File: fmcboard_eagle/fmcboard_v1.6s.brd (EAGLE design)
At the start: 147 x 74 mm, 300 parts, among them IC1 OPA699ID, IC10 LM358, IC11 7805DT, IC12 SN74AUC2G66DCTR, IC13 SN74AUC2G66DCTR, IC14 SN74AUC2G66DCTR, IC15 SN74AUC2G66DCTR, IC16 DAC7578SPWR, IC17 SN74AUC2G66DCTR, IC18 SN74AUC2G66DCTR, IC19 SN74AUC2G66DCTR, IC2 DAC7578SPWR, IC20 SN74AUC2G66DCTR, IC21 74AUP2GU04GW, IC22 74AUP2GU04GW, IC23 74AUP2GU04GW, IC24 74AUP2GU04GW, IC25 MC7905ACD2TR4G, IC26 AMS1117-1.8, IC27 LM358, IC28 SN74AUC2G66DCTR, IC29 LM337KVURG3, IC3 LTC6229IMS8E#TRPBF, IC30 SN74AUC2G66DCTR, IC31 SN74AUC2G66DCTR, IC32 SN74AUC2G66DCTR, IC33 LTC6229IMS8E#TRPBF, IC34 74AUP2GU04GW, IC35 74AUP2GU04GW, IC36 TPS5430DDAR, IC37 TPS5430DDAR, IC4 OPA695IDR, IC5 LTC6229IMS8E#TRPBF, IC6 OPA695IDR, IC7 OPA699ID, IC8 LM358, IC9 LM358, J1 8pin, J12 4p-2.54, J13 4p-2.54, J2 ASP-134604-01, J3 2p-2.54, J4 4p-2.54, J5 4p-2.54, J8 4p-2.54, J9 2p-2.54

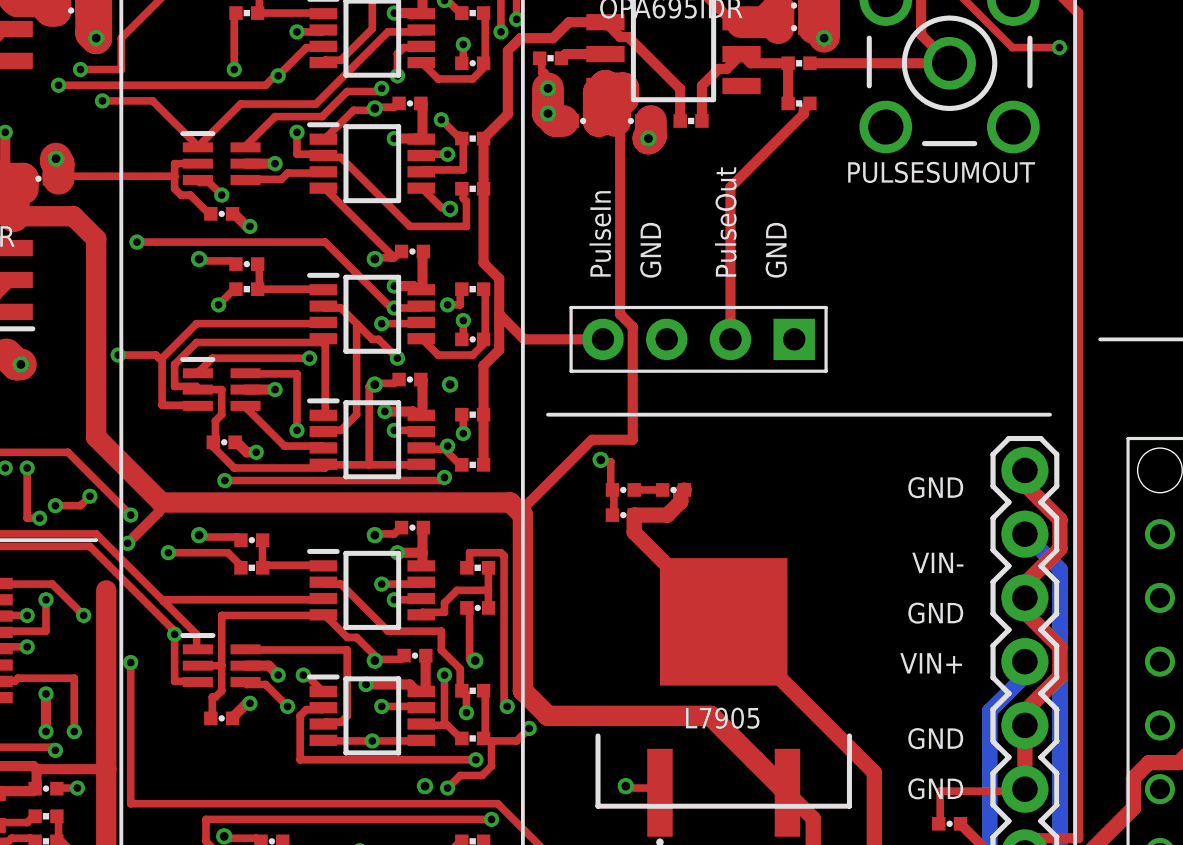
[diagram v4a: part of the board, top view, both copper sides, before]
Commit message: remove pulsein hole
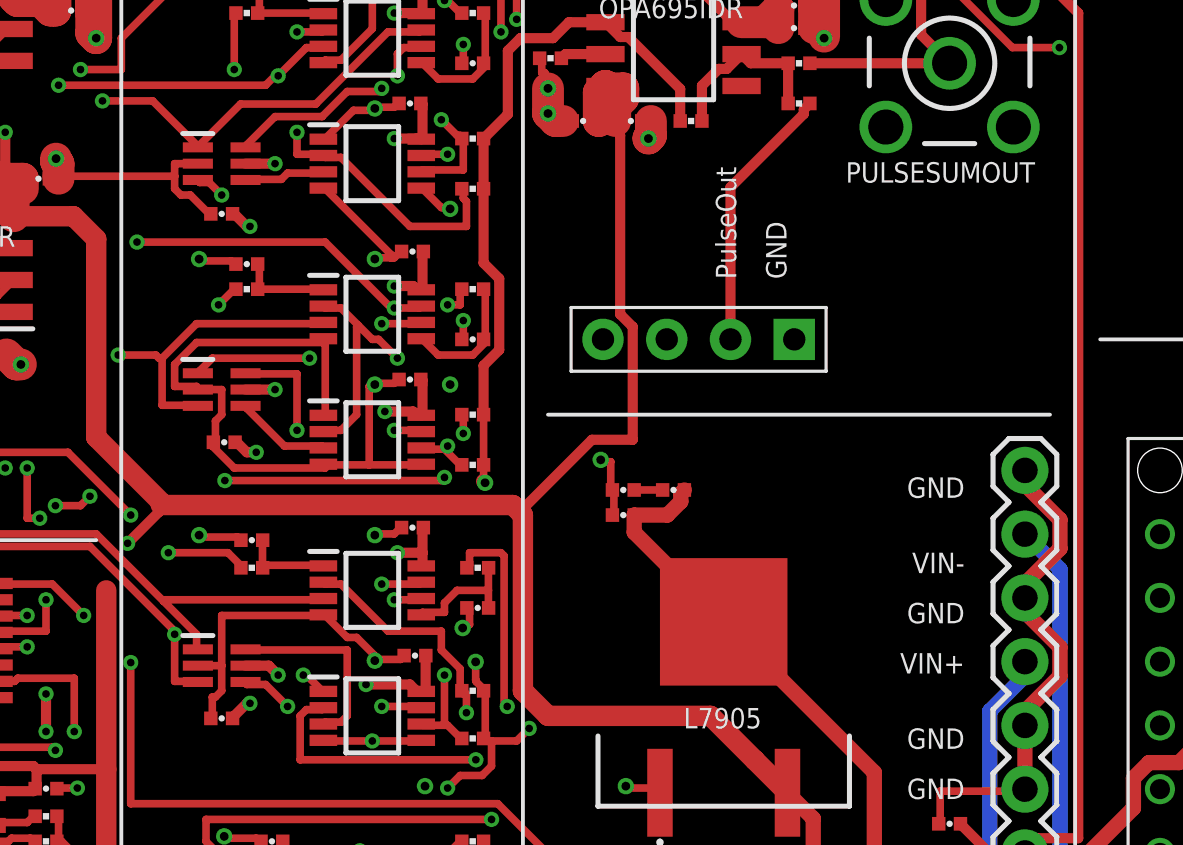
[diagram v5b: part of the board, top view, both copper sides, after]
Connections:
- net GND: no longer J13.3
- net PULSESUMIN: no longer J13.4
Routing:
- net PULSESUMIN: track 111.4 -> 108.3 mm, vias 6 -> 8
- net GND: track 529.4 -> 527.5 mm
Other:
- board text removed: "PulseIn"
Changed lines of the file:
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@@
 <text x="22.4" y="63.1" size="0.8128" layer="21" rot="R180">12V</text>
 <text x="100.6" y="35.5" size="0.8128" layer="21" rot="R180">GND</text>
-<text x="88.5" y="55.4" size="0.8128" layer="21" rot="R90">GND</text>
 <text x="100.6" y="47.5" size="0.8128" layer="21" rot="R180">GND</text>
 <text x="7" y="1" size="1.27" layer="21" rot="R90">C10GX FMC breakout, v1.652s
@@
 <text x="100.6" y="32.5" size="0.8128" layer="21" rot="R180">+VS 5</text>
 <text x="100.6" y="30.5" size="0.8128" layer="21" rot="R180">AR 5V</text>
-<text x="86.5" y="55.4" size="0.8128" layer="21" rot="R90">PulseIn</text>
 <text x="93.5" y="55.4" size="0.8128" layer="21" rot="R90">GND</text>
 <text x="91.5" y="55.4" size="0.8128" layer="21" rot="R90">PulseOut</text>
@@
 <contactref element="PULSESUMOUT" pad="5"/>
 <contactref element="PULSESUMOUT" pad="3"/>
-<contactref element="J1" pad="8"/>
 <contactref element="C6" pad="2"/>
 <contactref element="C15" pad="2"/>
@@
 <contactref element="C74" pad="2"/>
 <contactref element="J13" pad="1"/>
-<contactref element="J13" pad="3"/>
 <contactref element="J5" pad="4"/>
 <contactref element="R10" pad="1"/>
@@
 <wire x1="141.635" y1="41.365" x2="141" y2="42" width="0.6096" layer="1"/>
 <wire x1="104.397" y1="45.8186625" x2="104.397" y2="44.6613375" width="0.6096" layer="1"/>
-<wire x1="103" y1="47.78" x2="103" y2="47.2156625" width="0.6096" layer="1"/>
 <wire x1="103" y1="43.2643375" x2="103" y2="42.7" width="0.6096" layer="1"/>
 <wire x1="103" y1="47.2156625" x2="104.397" y2="45.8186625" width="0.6096" layer="1"/>
@@
 <via x="81.1" y="17.2" extent="1-16" drill="0.35"/>
 <via x="81.1" y="28.2" extent="1-16" drill="0.35"/>
-<via x="81.1" y="40.2" extent="1-16" drill="0.35"/>
+<via x="80.6" y="41.5" extent="1-16" drill="0.35"/>
 <via x="80.1" y="51.2" extent="1-16" drill="0.35"/>
 <via x="80.1" y="58.2" extent="1-16" drill="0.35"/>
@@
 <wire x1="78.125" y1="45.5" x2="78.16693125" y2="45.5" width="0.3048" layer="1"/>
 <wire x1="77.125" y1="45.25" x2="77.1" y2="45.2" width="0.3048" layer="1"/>
-<wire x1="80.875" y1="40.25" x2="80.875" y2="42.25" width="0.3048" layer="1"/>
-<wire x1="81" y1="40.25" x2="80.875" y2="40.25" width="0.3048" layer="1"/>
+<wire x1="80.875" y1="41.6375" x2="80.875" y2="42.25" width="0.3048" layer="1"/>
 <wire x1="80.875" y1="42.25" x2="80.76693125" y2="42.3" width="0.3048" layer="1"/>
-<wire x1="81" y1="40.25" x2="81.1" y2="40.2" width="0.3048" layer="1"/>
+<wire x1="80.875" y1="41.6375" x2="80.6" y2="41.5" width="0.3048" layer="1"/>
 <wire x1="58.625" y1="62.625" x2="58.63306875" y2="62.6" width="0.3048" layer="1"/>
 <wire x1="58.625" y1="62.625" x2="59.0001" y2="62.6" width="0.3048" layer="1"/>
@@
 <wire x1="84" y1="16.375" x2="83.96693125" y2="16.3" width="0.3048" layer="1"/>
 <wire x1="84" y1="16.375" x2="84.005090625" y2="16.369909375" width="0.3048" layer="1"/>
+<contactref element="J1" pad="8"/>
 </signal>
 <signal name="IO1">
@@
 <wire x1="84" y1="38" x2="83" y2="39" width="0.8128" layer="1"/>
 <wire x1="83" y1="39" x2="83" y2="46" width="0.8128" layer="1"/>
-<wire x1="83" y1="46" x2="82.875" y2="46.125" width="0.8128" layer="1"/>
-<wire x1="82.875" y1="46.125" x2="82.5" y2="46.5" width="0.8128" layer="1"/>
-<wire x1="82.5" y1="46.5" x2="68.6" y2="46.5" width="0.8128" layer="1"/>
+<wire x1="82.875" y1="46.125" x2="83" y2="46" width="0.8128" layer="1"/>
+<wire x1="82.875" y1="46.125" x2="82.6" y2="46.4" width="0.8128" layer="1"/>
+<wire x1="82.6" y1="46.4" x2="68.573334375" y2="46.4" width="0.8128" layer="1"/>
 <wire x1="68.6" y1="46.5" x2="66" y2="49.1" width="0.8128" layer="1"/>
 <wire x1="66" y1="49.1" x2="66" y2="57" width="0.8128" layer="1"/>
@@
 <wire x1="68.5" y1="46.125" x2="67.25" y2="44.875" width="0.4064" layer="1"/>
 <wire x1="57.5" y1="31.5" x2="57.375" y2="31.375" width="0.4064" layer="15"/>
-<wire x1="68.5" y1="46.125" x2="68.6" y2="46.5" width="0.4064" layer="1"/>
+<wire x1="68.5" y1="46.125" x2="68.573334375" y2="46.4" width="0.4064" layer="1"/>
+<wire x1="68.573334375" y1="46.4" x2="68.6" y2="46.5" width="0.4064" layer="1"/>
 <via x="54.5" y="34.25" extent="1-16" drill="0.3048"/>
 <via x="57.375" y="31.375" extent="1-16" drill="0.3048"/>
@@
 <contactref element="R113" pad="1"/>
 <contactref element="R114" pad="1"/>
-<contactref element="J13" pad="4"/>
 <wire x1="86.289" y1="65.635" x2="86.8784" y2="65.0456" width="0.4064" layer="1"/>
 <wire x1="86.8784" y1="65.0456" x2="87.20029375" y2="65.0456" width="0.4064" layer="1"/>
@@
 <wire x1="81.43306875" y1="56.0439125" x2="82.0566375" y2="55.42034375" width="0.4064" layer="1"/>
 <wire x1="82.0566375" y1="52.57965625" x2="81.43306875" y2="51.9560875" width="0.4064" layer="1"/>
-<wire x1="82.0566375" y1="55.42034375" x2="82.0566375" y2="54" width="0.4064" layer="1"/>
-<wire x1="82.0566375" y1="54" x2="82.0566375" y2="52.57965625" width="0.4064" layer="1"/>
-<wire x1="81.43306875" y1="50" x2="81.43306875" y2="48" width="0.4064" layer="1"/>
-<wire x1="86.19" y1="53" x2="83.0566375" y2="53" width="0.4064" layer="1"/>
-<wire x1="83.0566375" y1="53" x2="82.0566375" y2="54" width="0.4064" layer="1"/>
+<wire x1="82.0566375" y1="55.42034375" x2="82.0566375" y2="52.57965625" width="0.4064" layer="1"/>
 <wire x1="81.43306875" y1="59" x2="81.43306875" y2="61" width="0.4064" layer="1"/>
 <wire x1="81.5" y1="5" x2="81.5" y2="3" width="0.3048" layer="1"/>
@@
 <wire x1="81.375" y1="26.125" x2="82" y2="25.5" width="0.3048" layer="15"/>
 <wire x1="81.375" y1="26.125" x2="81.375" y2="26.25" width="0.3048" layer="15"/>
-<wire x1="86.125" y1="49.125" x2="86.125" y2="53" width="0.3048" layer="15"/>
-<wire x1="83.25" y1="46.25" x2="86.125" y2="49.125" width="0.3048" layer="15"/>
 <wire x1="83.25" y1="37.5" x2="83.25" y2="46.25" width="0.3048" layer="15"/>
 <wire x1="82.75" y1="37" x2="83.25" y2="37.5" width="0.3048" layer="1"/>
 <wire x1="81.75" y1="37" x2="82.75" y2="37" width="0.3048" layer="1"/>
-<wire x1="86.125" y1="53" x2="86.19" y2="53" width="0.3048" layer="15"/>
 <via x="82" y="5.625" extent="1-16" drill="0.3048"/>
 <via x="82" y="14.625" extent="1-16" drill="0.3048"/>
@@
 <via x="81.375" y="26.25" extent="1-16" drill="0.3048"/>
 <via x="83.25" y="37.5" extent="1-16" drill="0.3048"/>
+<wire x1="81.43306875" y1="47.34593125" x2="81.4928" y2="47.2862" width="0.6096" layer="1"/>
+<via x="81.4928" y="47.2862" extent="1-16" drill="0.35"/>
+<wire x1="81.4928" y1="47.2862" x2="81.5154" y2="47.2636" width="0.6096" layer="15"/>
+<wire x1="81.5154" y1="47.2636" x2="81.5154" y2="42.91198125" width="0.3048" layer="15"/>
+<wire x1="81.5154" y1="42.91198125" x2="81.2928" y2="42.68938125" width="0.3048" layer="15"/>
+<wire x1="81.2928" y1="42.68938125" x2="81.2928" y2="41" width="0.3048" layer="15"/>
+<wire x1="81.2928" y1="41" x2="81.2928" y2="40.9" width="0.3048" layer="15"/>
+<wire x1="81.2928" y1="41" x2="81.1178" y2="40.825" width="0.3048" layer="15"/>
+<wire x1="81.1178" y1="40.825" x2="81.1178" y2="40.15126875" width="0.3048" layer="15"/>
+<via x="81.1178" y="40.15126875" extent="1-16" drill="0.35"/>
+<wire x1="81.1178" y1="40.15126875" x2="81.1178" y2="39.4212" width="0.3048" layer="1"/>
+<wire x1="81.1178" y1="39.4212" x2="81.1397" y2="39.3993" width="0.3048" layer="1"/>
+<wire x1="81.1397" y1="39.3993" x2="81.1397" y2="39.3603" width="0.3048" layer="1"/>
+<wire x1="81.1397" y1="39.3603" x2="81.5" y2="39" width="0.3048" layer="1"/>
+<wire x1="81.43306875" y1="50" x2="81.43306875" y2="48" width="0.3048" layer="1"/>
+<wire x1="81.43306875" y1="48" x2="81.43306875" y2="47.34593125" width="0.3048" layer="1"/>
 </signal>
 <signal name="PULSESUMOUT">

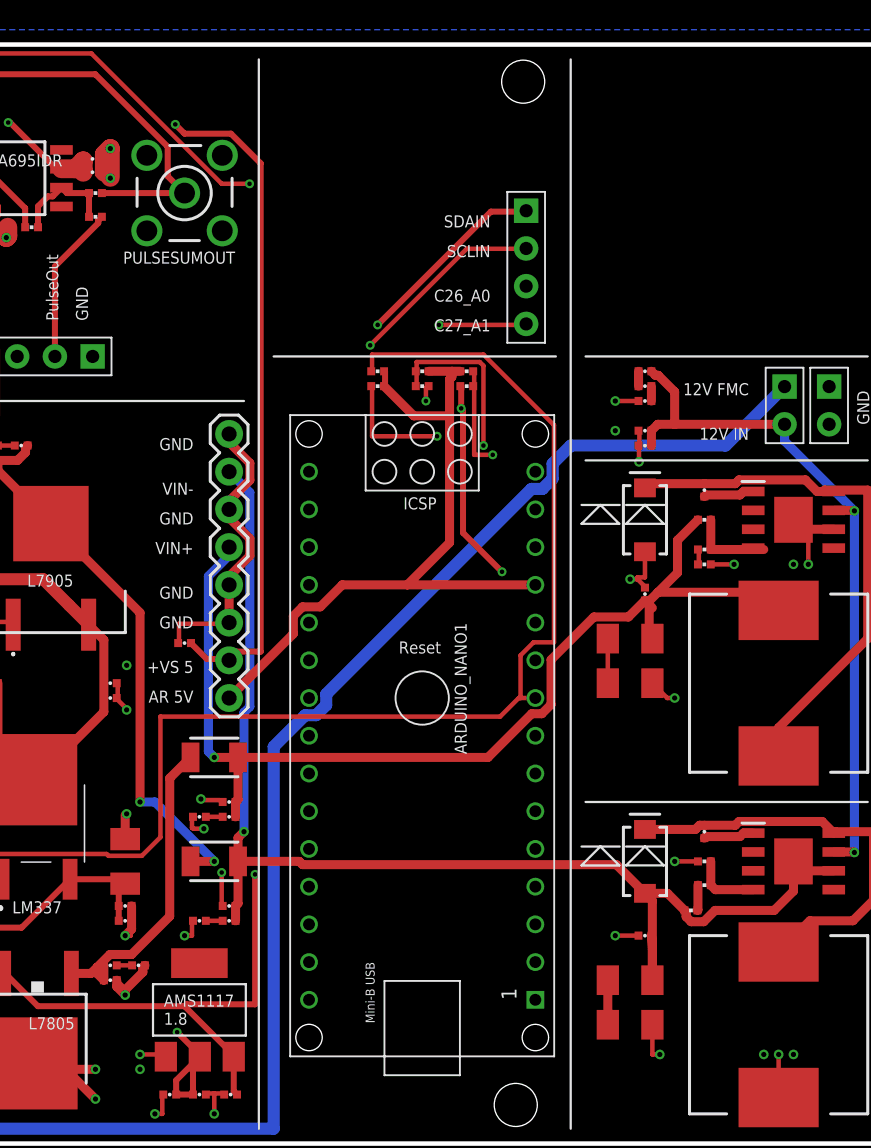
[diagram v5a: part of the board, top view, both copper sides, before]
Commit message: remove sdain sclin c26 c27 holes clean up +-7 V schematic
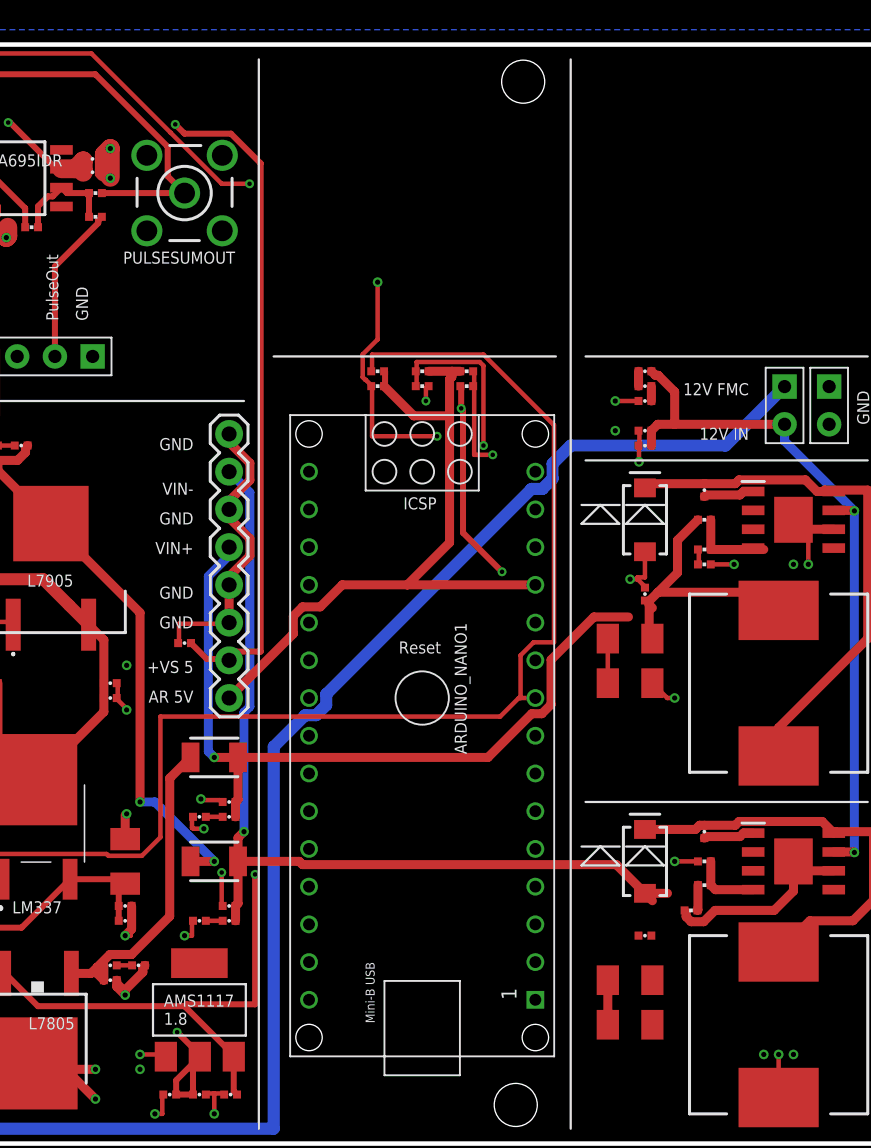
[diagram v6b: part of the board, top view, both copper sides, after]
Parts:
- removed J4: 4p-2.54, Seeed-Connector:H4-2.54
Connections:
- net C26: no longer J4.3
- net C27: no longer J4.4
- net SCLIN: no longer J4.2
- net SDAIN: no longer J4.1
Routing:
- net SDAIN: track 180.0 -> 158.8 mm, vias 4 -> 3
- net SCLIN: track 172.9 -> 154.4 mm, vias 5 -> 4
- net VIN-: track 85.4 -> 75.3 mm
- net C27: track 181.9 -> 173.6 mm, vias 3 -> 2
- net C26: track 189.0 -> 183.5 mm
- net GND: track 527.5 -> 523.4 mm, vias 135 -> 133
- net VIN+: track 74.7 -> 71.2 mm
- net AR_SDAIN2: track 134.5 -> 132.4 mm, vias 5 -> 6
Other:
- board text removed: "C26_A0"
- board text removed: "C27_A1"
- board text removed: "SCLIN"
- board text removed: "SDAIN"

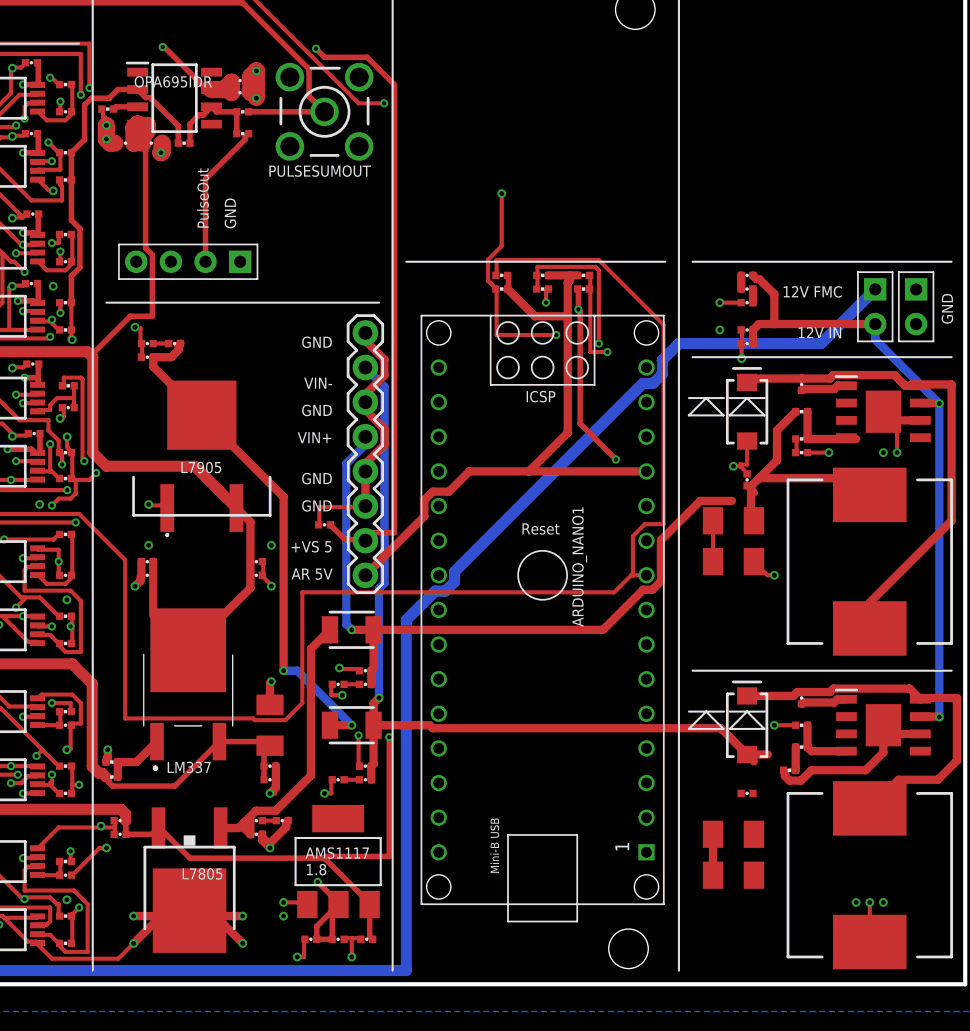
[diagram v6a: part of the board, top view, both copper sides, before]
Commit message: 0805 10uF
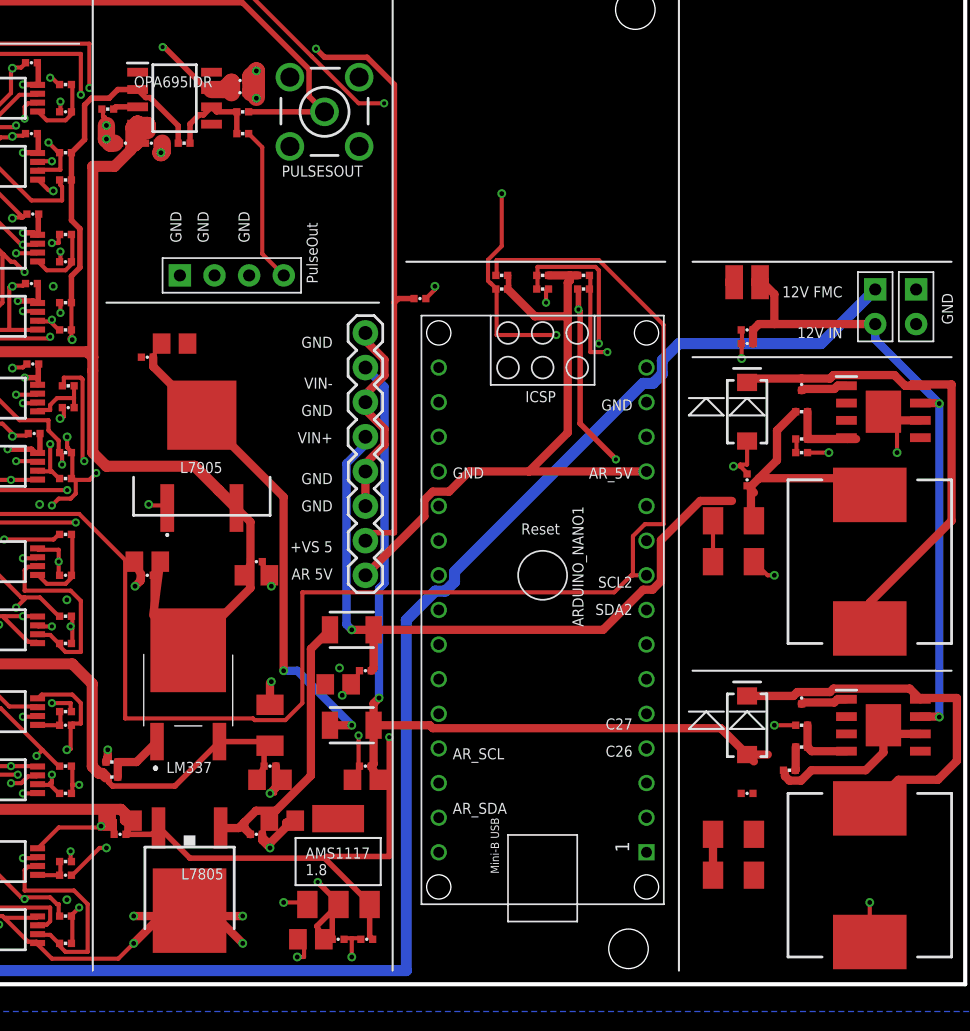
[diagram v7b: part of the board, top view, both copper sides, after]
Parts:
- removed C118, C119, C2, C40, C80: 10uF, passives:0402_CAP
- C1, C110, C111, C120, C34, C38, C39, C41, C64, C77, C86: device passives:0402_CAP -> rcl:C0805
- moved C6 18.0 mm to (107.0, 50.3), turned to 0 degrees
- moved J13 3.35 mm to (93.2, 52.0), turned to 90 degrees
- renumbered PULSESUMOUT to PULSESOUT
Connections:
- removed net N$35: J13.2, R71.1
- removed net N$38: C1.1, C118.2
- removed net N$39: C119.2, C41.1
- removed net N$52: C120.2, C80.1
- removed net N$58: C110.1, C2.2
- removed net N$59: C111.1, C40.2
- new net N$57: J13.4, R71.1
- net GND: now also C111.1, C120.2, C41.1, J13.2, J13.3; no longer C119.1, C40.1, C80.2
- net VIN+: now also C1.1; no longer C118.1
- net VIN+CLEAN: now also C110.1; no longer C2.1
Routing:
- net N$57: track 0.00 -> 11.5 mm
- net N$35: track 10.7 -> 0.00 mm
- net GND: track 523.4 -> 515.0 mm, vias 133 -> 124
- net VIN-CLEAN: track 37.8 -> 35.2 mm
- net VS-: track 252.4 -> 251.0 mm
- net N$59: track 1.13 -> 0.00 mm
- net N$39: track 1.13 -> 0.00 mm
- net N$38: track 1.13 -> 0.00 mm
- net N$52: track 1.11 -> 0.00 mm
- net N$58: track 1.03 -> 0.00 mm
- net VIN+CLEAN: track 21.6 -> 20.6 mm
- net VIN+: track 71.2 -> 70.2 mm
- net VS+: track 379.2 -> 378.3 mm
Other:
- board text added: "AR_5V"
- board text added: "AR_SCL"
- board text added: "AR_SDA"
- board text added: "C26"
- board text added: "C27"
- board text added: "SCL2"
- board text added: "SDA2"
